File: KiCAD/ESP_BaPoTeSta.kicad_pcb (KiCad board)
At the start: 2 copper layers, 39.4 x 49.5 mm, 32 parts, among them P1 Progr, P10 CONN_01X04, P13 CONN_01X03, P15 CONN_01X04, P2 Battery, P4 Upload, P5 Config, P9 CONN_01X04, Q1 IRLML6302, U1 MCP1700-330, U2 ESP-12

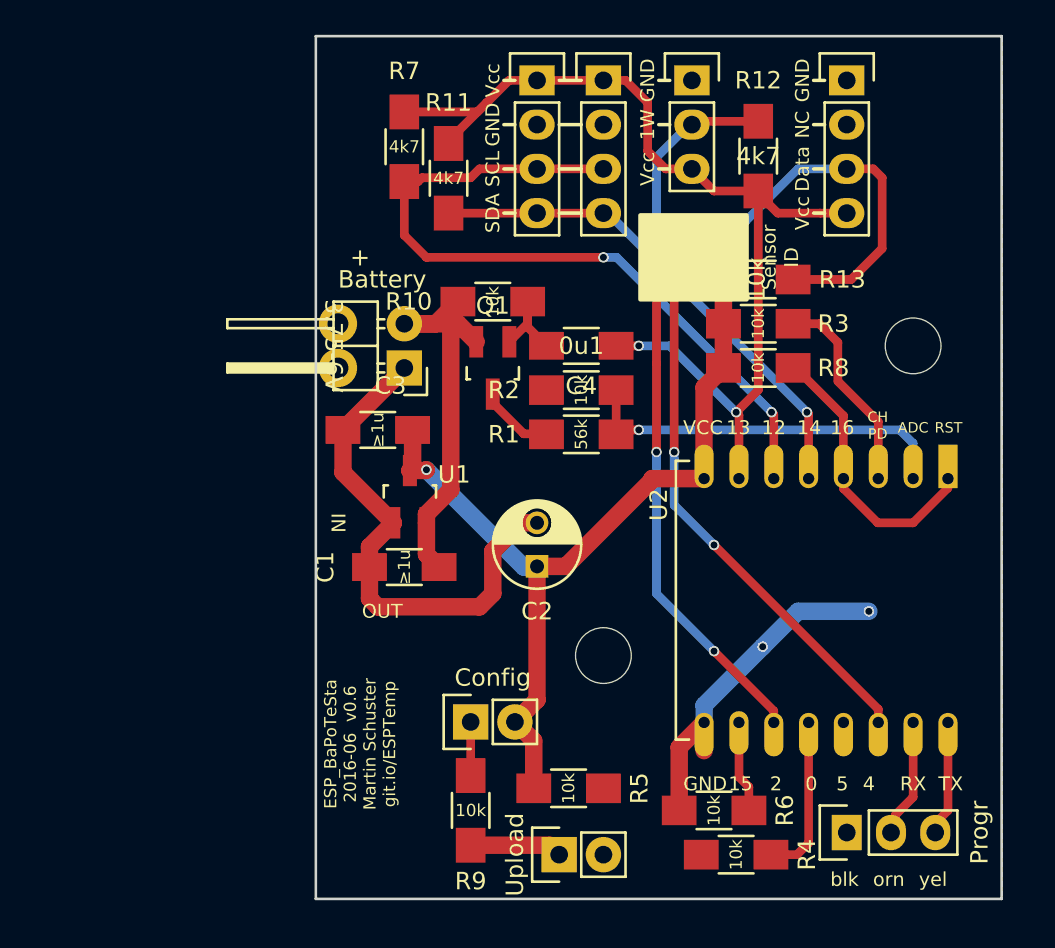
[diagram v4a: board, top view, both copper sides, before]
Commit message: WIP: PCB: battery charger
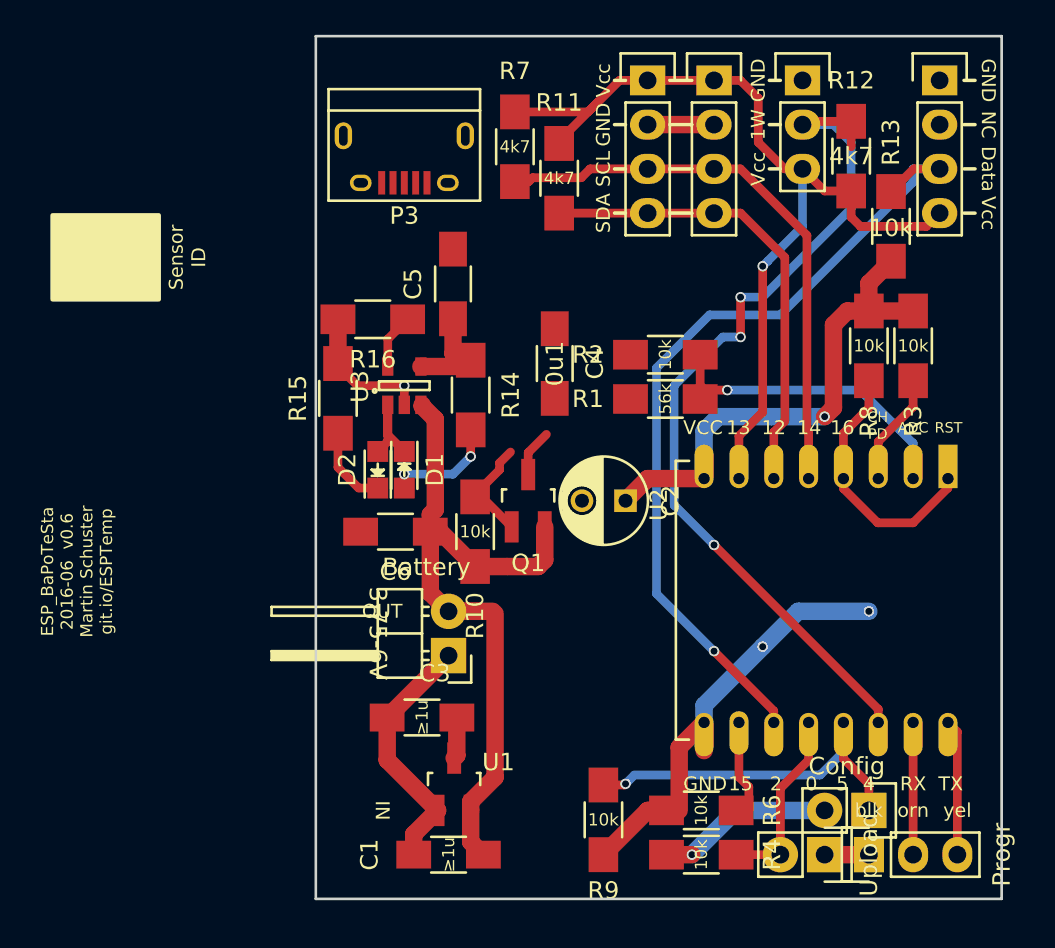
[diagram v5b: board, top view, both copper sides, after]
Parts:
- removed R5: 10k, Resistors_SMD:R_1206_HandSoldering
- removed REF** (x2): MountingHole_3.2mm_M3_ISO7380, Mounting_Holes:MountingHole_3.2mm_M3_ISO7380
- removed REF** (x2): MountingHole_2.2mm_M2, Mounting_Holes:MountingHole_2.2mm_M2
- added C5: 4u7, Capacitors_SMD:C_1206_HandSoldering, F.Cu at (131.1, 80.3)
- added C6: 4u7, Capacitors_SMD:C_1206_HandSoldering, F.Cu at (127.8, 94.5)
- added D1: Red, LEDs:LED_0805, F.Cu at (128.3, 90.9)
- added D2: Blu, LEDs:LED_0805, F.Cu at (126.7, 90.9)
- added P3: MicroUSB, Connect:USB_Micro-B, F.Cu at (128.3, 72.9)
- added R14: 220, Resistors_SMD:R_1206_HandSoldering, F.Cu at (132.1, 86.6)
- added R15: 220, Resistors_SMD:R_1206_HandSoldering, F.Cu at (124.5, 86.8)
- added R16: 2k2, Resistors_SMD:R_1206_HandSoldering, F.Cu at (126.5, 82.3)
- added U3: MCP73831-2-OT, TO_SOT_Packages_SMD:SOT-23-5, F.Cu at (128.3, 86.1)
- moved P5 23.4 mm to (154.9, 110.5), turned to 270 degrees
- moved C3 16.7 mm to (129.3, 105.2)
- moved C1 16.7 mm to (130.8, 113.0)
- moved U1 16.7 mm to (131.1, 109.0)
- moved P2 16.7 mm to (130.8, 101.6)
- moved P4 15.2 mm to (152.4, 113.0), turned to 270 degrees
- moved R10 13.2 mm to (132.3, 94.5), turned to 90 degrees
- moved R3 8.98 mm to (157.5, 83.8), turned to 90 degrees
- moved R13 8.21 mm to (156.2, 77.0), turned to 270 degrees
- moved Q1 7.89 mm to (135.4, 92.7), turned to 0 degrees
- moved R9 7.64 mm to (139.7, 111.0)
- moved R8 6.48 mm to (154.9, 83.8), turned to 270 degrees
- moved P10 6.35 mm to (146.1, 68.6)
- moved P9 6.35 mm to (142.2, 68.6)
- moved P13 6.35 mm to (151.1, 68.6)
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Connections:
- net Net-(P1-Pad2) renamed RXD
- net Net-(P1-Pad3) renamed TXD
- U2 pad 5: SDA -> SCL
- U2 pad 6: SCL -> SDA
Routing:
- net /GPIO4: track 3.08 -> 21.9 mm, vias 0 -> 1
- net +BATT: track 23.1 -> 41.2 mm
- net SCL: track 44.0 -> 32.6 mm, vias 2 -> 0
- net VCC: track 49.4 -> 41.3 mm, vias 1 -> 2
- net DHTData: track 55.6 -> 48.1 mm, vias 3 -> 1
- net 1Wire: track 44.4 -> 51.3 mm
- net /Rred: track 0.00 -> 6.55 mm, vias 0 -> 2
- net /Vin: track 0.00 -> 6.18 mm
- net /Status: track 0.00 -> 5.99 mm
- net PwrSens: track 59.9 -> 54.0 mm, vias 2 -> 1
- net /CH_PD: track 11.8 -> 6.45 mm
- net /Rblu: track 0.00 -> 4.74 mm
- net ADC: track 22.0 -> 18.5 mm
- net Net-(R16-Pad1): track 0.00 -> 3.18 mm
- net SDA: track 29.2 -> 27.0 mm, vias 1 -> 0
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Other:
- board text removed: "+"

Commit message: WIP: PCB: redesign nearly finished
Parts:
- removed C6: 4u7, Capacitors_SMD:C_1206_HandSoldering
- P2: footprint Pin_Headers:Pin_Header_Angled_1x02 -> Pin_Headers:Pin_Header_Straight_1x02
- moved C1 19.8 mm to (130.0, 93.2), turned to 270 degrees
- moved U1 13.0 mm to (135.6, 96.8), turned to 270 degrees
- moved C3 13.0 mm to (134.9, 93.5)
- moved R10 6.62 mm to (135.9, 88.9)
- moved P2 5.99 mm to (127.3, 96.8), turned to 270 degrees
- moved Q1 5.79 mm to (140.0, 89.2), turned to 270 degrees
- moved R14 4.83 mm to (127.5, 85.1)
- moved C4 3.89 mm to (140.7, 84.1), turned to 180 degrees
- moved R16 3.85 mm to (130.3, 82.5), turned to 90 degrees
- moved U3 3.75 mm to (131.6, 87.9)
- moved C5 2.90 mm to (132.8, 82.5)
- moved R2 2.87 mm to (145.3, 82.3), turned to 90 degrees
- moved P3 2.05 mm to (127.3, 74.7), turned to 270 degrees
- moved D2 1.85 mm to (125.0, 91.4), turned to 270 degrees
- moved R15 1.82 mm to (125.0, 85.1)
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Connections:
- P2 pad 1: GND -> +BATT
- P2 pad 2: +BATT -> GND
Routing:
- net VCC: track 41.3 -> 66.8 mm, vias 2 -> 4
- net +BATT: track 41.2 -> 25.0 mm
- net /Vin: track 6.18 -> 21.1 mm, vias 0 -> 2
- net GND: track 53.7 -> 42.9 mm, vias 3 -> 4
- net PwrSens: track 54.0 -> 63.1 mm
- net 1Wire: track 51.3 -> 48.2 mm
- net /Rred: track 6.55 -> 3.51 mm, vias 2 -> 0
- net /Rblu: track 4.74 -> 2.79 mm
- net /Status: track 5.99 -> 7.85 mm
- net /G: track 6.23 -> 7.34 mm
- net Net-(R16-Pad1): track 3.18 -> 2.37 mm
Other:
- board text added: "ESP_BaPoTeSta 2016-11 v0.6 Martin Schuster git.io/ESPTemp"
- board text removed: "IN"
- board text removed: "OUT"

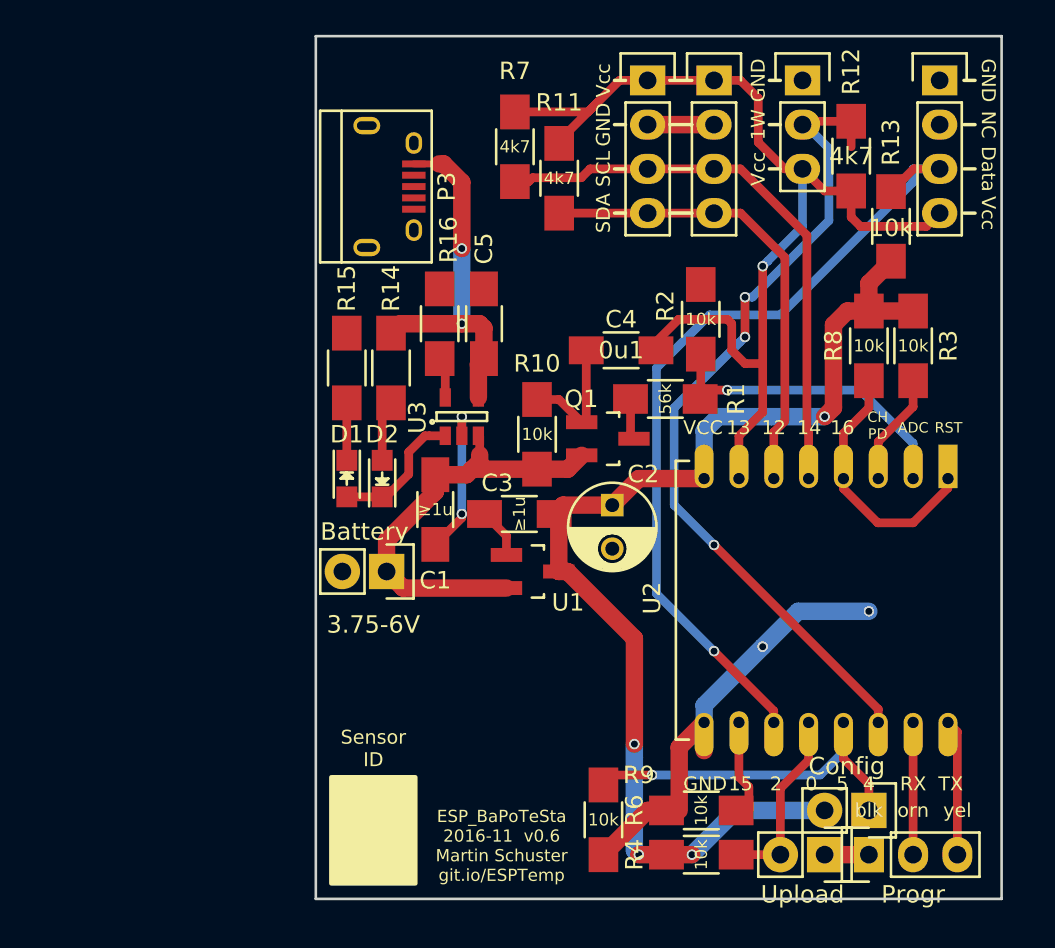
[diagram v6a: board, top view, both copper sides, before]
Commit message: DOC: PCB: silkscreen improvements
Fix size/position of labels
swap GPIO 4<->5 labels
add header diagram
fix voltage labels (ESP needs 2.5V in, so 3.0V battery is ok)
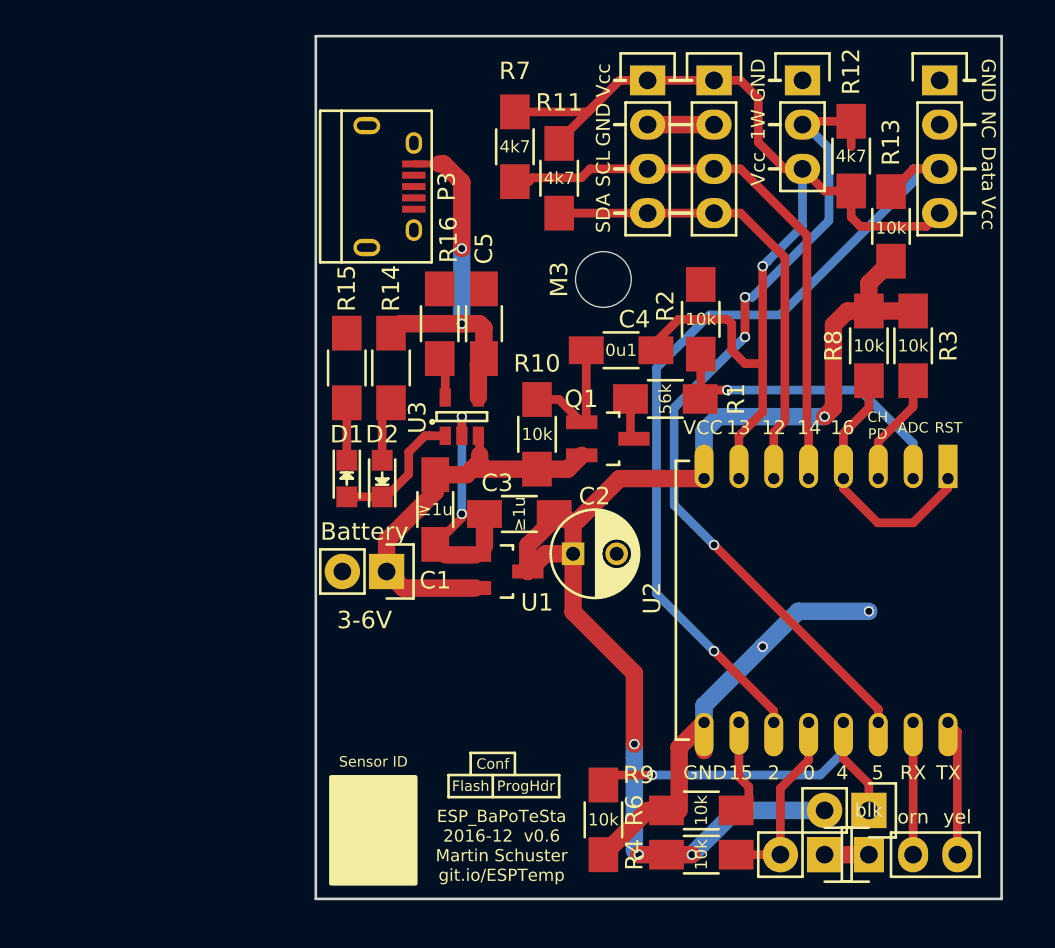
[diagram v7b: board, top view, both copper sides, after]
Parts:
- added M3: MountingHole_3.2mm_M3_ISO7380, Mounting_Holes:MountingHole_3.2mm_M3_ISO7380, F.Cu at (139.7, 80.0)
- P1: value Progr -> ProgHdr
- P4: value Upload -> Flash
- P5: value Config -> Conf
- moved C2 3.58 mm to (138.0, 95.8), turned to 0 degrees
- moved U1 1.78 mm to (133.9, 96.8)
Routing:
- net VCC: track 66.8 -> 72.9 mm
- net GND: track 42.9 -> 46.5 mm
- net +BATT: track 25.0 -> 23.2 mm
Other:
- board text added: "1Wire"
- board text added: "2.5-3.8V"
- board text added: "3-6V"
- board text added: "ESP_BaPoTeSta 2016-12 v0.6 Martin Schuster git.io/ESPTemp"
- board text added: "Flash"
- board text added: "PwrSens"
- board text removed: "1-Wire"
- board text removed: "3.3V"
- board text removed: "3.75-6V"
- board text removed: "ESP_BaPoTeSta 2016-06 v0.6 Martin Schuster git.io/ESPTemp"
- board text removed: "ESP_BaPoTeSta 2016-11 v0.6 Martin Schuster git.io/ESPTemp"
- board text removed: "PwrSnsr"
- board text removed: "Upload"

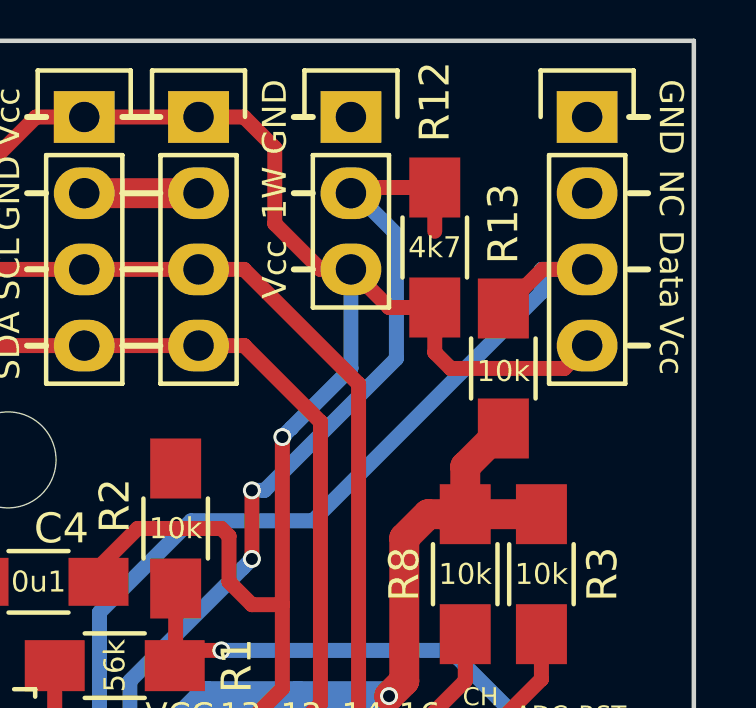
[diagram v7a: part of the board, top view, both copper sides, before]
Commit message: ENH: PCB: fix last 90deg-trace-bend
fixes #29
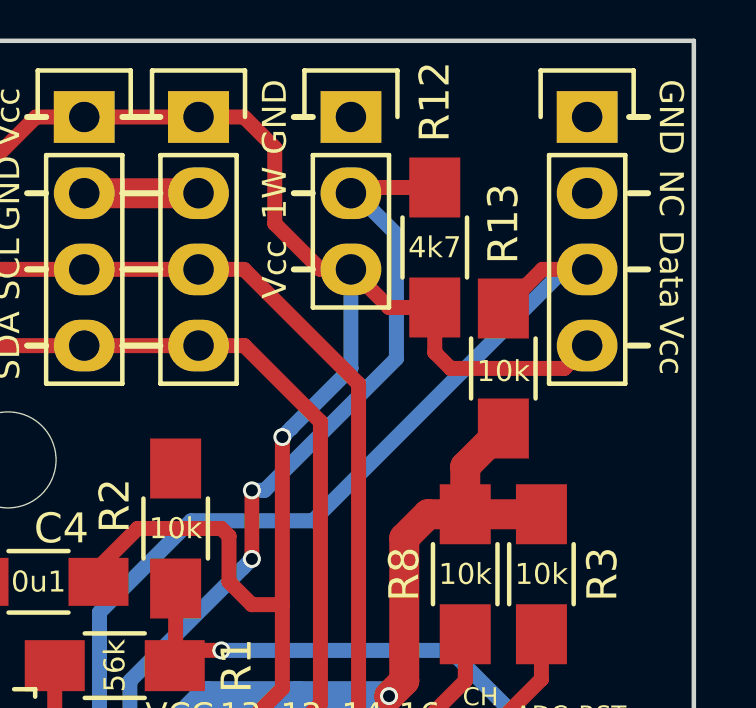
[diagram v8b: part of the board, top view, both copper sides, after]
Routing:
- net 1Wire: track 48.2 -> 46.7 mm
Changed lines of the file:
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@@
 (kicad_pcb (version 4) (host pcbnew 4.0.2+dfsg1-2~bpo8+1-stable)
   (general
-    (links 0)
+    (links 77)
     (no_connects 1)
-    (area 123.114999 65.964999 162.635001 115.645001)
+    (area 121.329 63.042619 168.455001 115.645001)
     (thickness 1.6)
     (drawings 95)
-    (tracks 230)
+    (tracks 227)
     (zones 0)
     (modules 36)
@@
   (segment (start 148.252264 81.026) (end 147.828 81.026) (width 0.5) (layer B.Cu) (net 10))
   (via (at 147.828 81.026) (size 0.6) (drill 0.4) (layers F.Cu B.Cu) (net 10))
-  (segment (start 153.924 72.39) (end 153.924 70.93) (width 0.5) (layer F.Cu) (net 10))
   (segment (start 153.924 70.93) (end 151.32 70.93) (width 0.5) (layer F.Cu) (net 10))
   (segment (start 151.32 70.93) (end 151.13 71.12) (width 0.5) (layer F.Cu) (net 10))
@@
   (segment (start 155.48 105.44) (end 155.48 104.68) (width 0.5) (layer F.Cu) (net 10))
   (segment (start 146.05 101.346) (end 142.748 98.044) (width 0.5) (layer B.Cu) (net 11))
+  (segment (start 158.242 73.66) (end 159.004 73.66) (width 0.5) (layer B.Cu) (net 11))
+  (segment (start 142.748 98.044) (end 142.748 85.09) (width 0.5) (layer B.Cu) (net 11))
   (segment (start 142.748 85.09) (end 145.796 82.042) (width 0.5) (layer B.Cu) (net 11))
-  (segment (start 142.748 98.044) (end 142.748 85.09) (width 0.5) (layer B.Cu) (net 11))
   (segment (start 145.796 82.042) (end 149.86 82.042) (width 0.5) (layer B.Cu) (net 11))
-  (segment (start 149.86 82.042) (end 157.48 74.422) (width 0.5) (layer B.Cu) (net 11))
-  (segment (start 157.48 74.422) (end 157.48 73.668) (width 0.5) (layer B.Cu) (net 11))
-  (segment (start 157.48 73.668) (end 157.488 73.66) (width 0.5) (layer B.Cu) (net 11))
-  (segment (start 157.488 73.66) (end 159.004 73.66) (width 0.5) (layer B.Cu) (net 11))
+  (segment (start 149.86 82.042) (end 158.242 73.66) (width 0.5) (layer B.Cu) (net 11))
   (segment (start 159.004 73.66) (end 157.512 73.66) (width 0.5) (layer F.Cu) (net 11))
   (segment (start 157.512 73.66) (end 156.21 74.962) (width 0.5) (layer F.Cu) (net 11))
